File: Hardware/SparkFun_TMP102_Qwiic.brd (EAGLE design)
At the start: 25.4 x 25.4 mm, 48 parts, among them J1 QWIIC, J2 QWIIC, J3 PTH, U1 TMP102

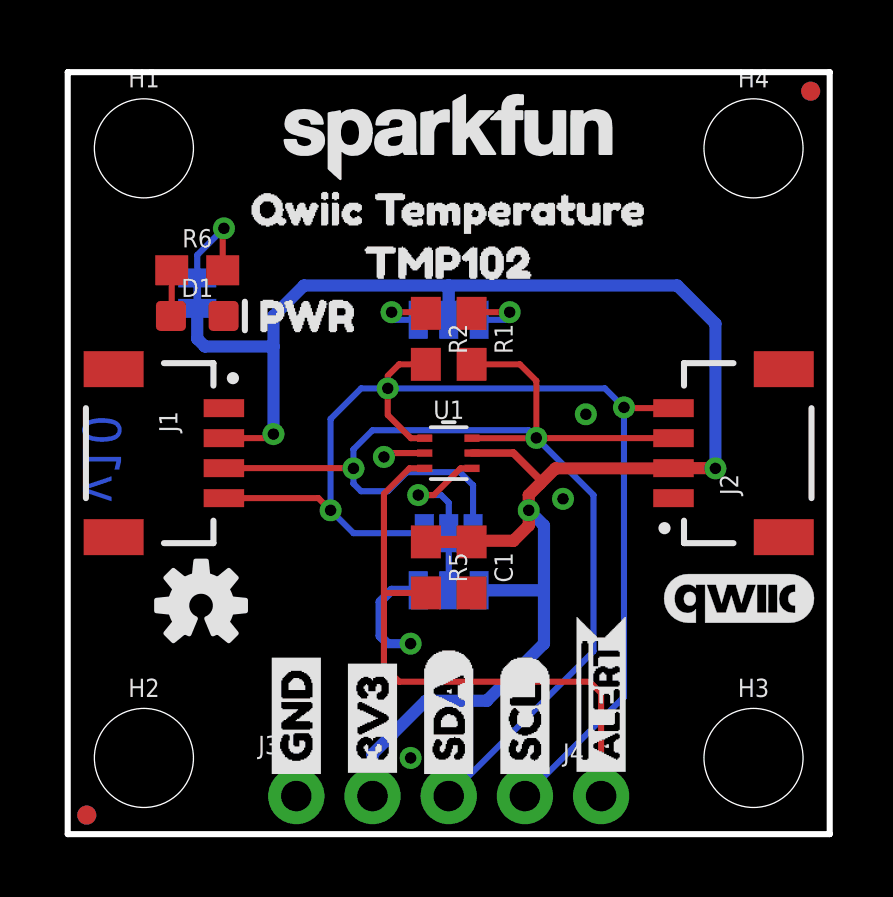
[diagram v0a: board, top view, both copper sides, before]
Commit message: v10 design review changes
- Added designer name to schematic
- Mitered I2C pull-up trances going to via
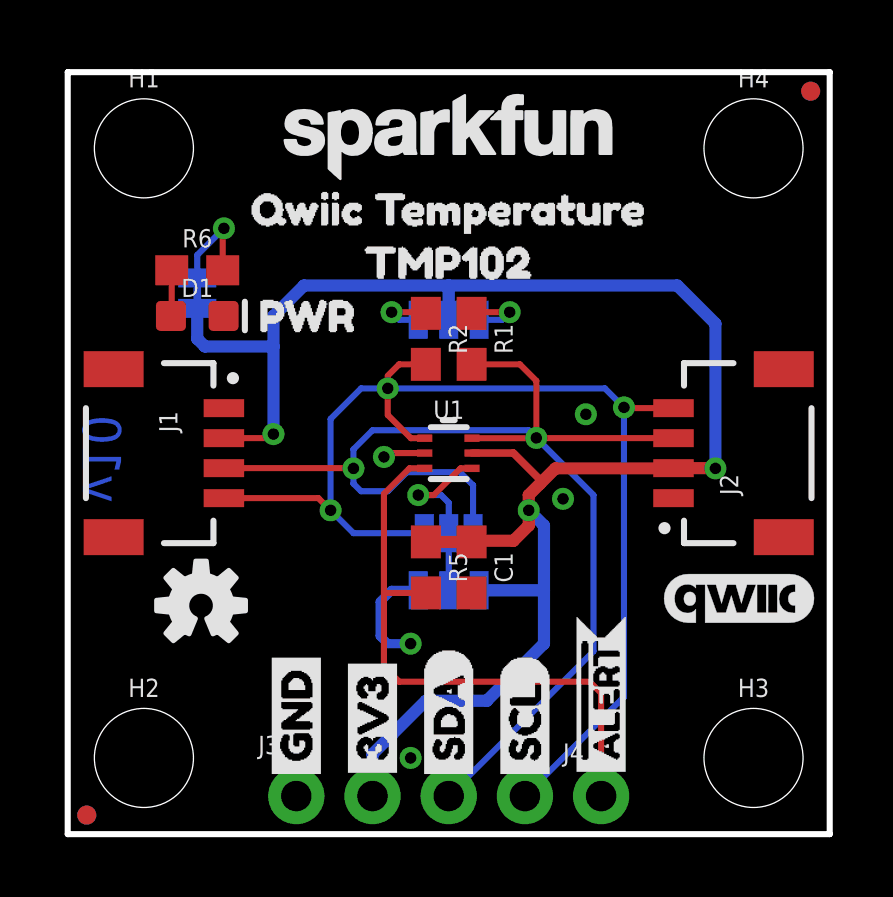
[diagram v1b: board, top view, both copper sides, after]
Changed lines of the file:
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@@
 <contactref element="JP3" pad="3"/>
 <contactref element="R1" pad="1"/>
-<wire x1="14.732" y1="17.399" x2="14.732" y2="17.145" width="0.2032" layer="16"/>
-<wire x1="13.716" y1="17.145" x2="14.732" y2="17.145" width="0.2032" layer="16"/>
+<wire x1="13.716" y1="17.145" x2="14.478" y2="17.145" width="0.2032" layer="16"/>
+<wire x1="14.478" y1="17.145" x2="14.732" y2="17.399" width="0.2032" layer="16"/>
 <via x="14.732" y="17.399" extent="1-16" drill="0.381"/>
 <wire x1="14.732" y1="17.399" x2="13.462" y2="17.399" width="0.2032" layer="1"/>
@@
 <contactref element="JP3" pad="1"/>
 <contactref element="R2" pad="1"/>
-<wire x1="11.684" y1="17.145" x2="10.795" y2="17.145" width="0.2032" layer="16"/>
-<wire x1="10.795" y1="17.145" x2="10.795" y2="17.399" width="0.2032" layer="16"/>
+<wire x1="11.684" y1="17.145" x2="11.049" y2="17.145" width="0.2032" layer="16"/>
+<wire x1="11.049" y1="17.145" x2="10.795" y2="17.399" width="0.2032" layer="16"/>
 <via x="10.795" y="17.399" extent="1-16" drill="0.381"/>
 <wire x1="10.795" y1="17.399" x2="11.938" y2="17.399" width="0.2032" layer="1"/>
